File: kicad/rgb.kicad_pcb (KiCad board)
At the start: 2 copper layers, 74 x 44 mm, 33 parts, among them J1 1935776, J2 Conn_01x05, J3 Conn_01x05, J4 Conn_01x04, J5 Conn_01x02, Q1 DMG9926USD, Q2 DMG9926USD, Q3 DMG9926USD, Q4 DMG9926USD, SW1 SW_Push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

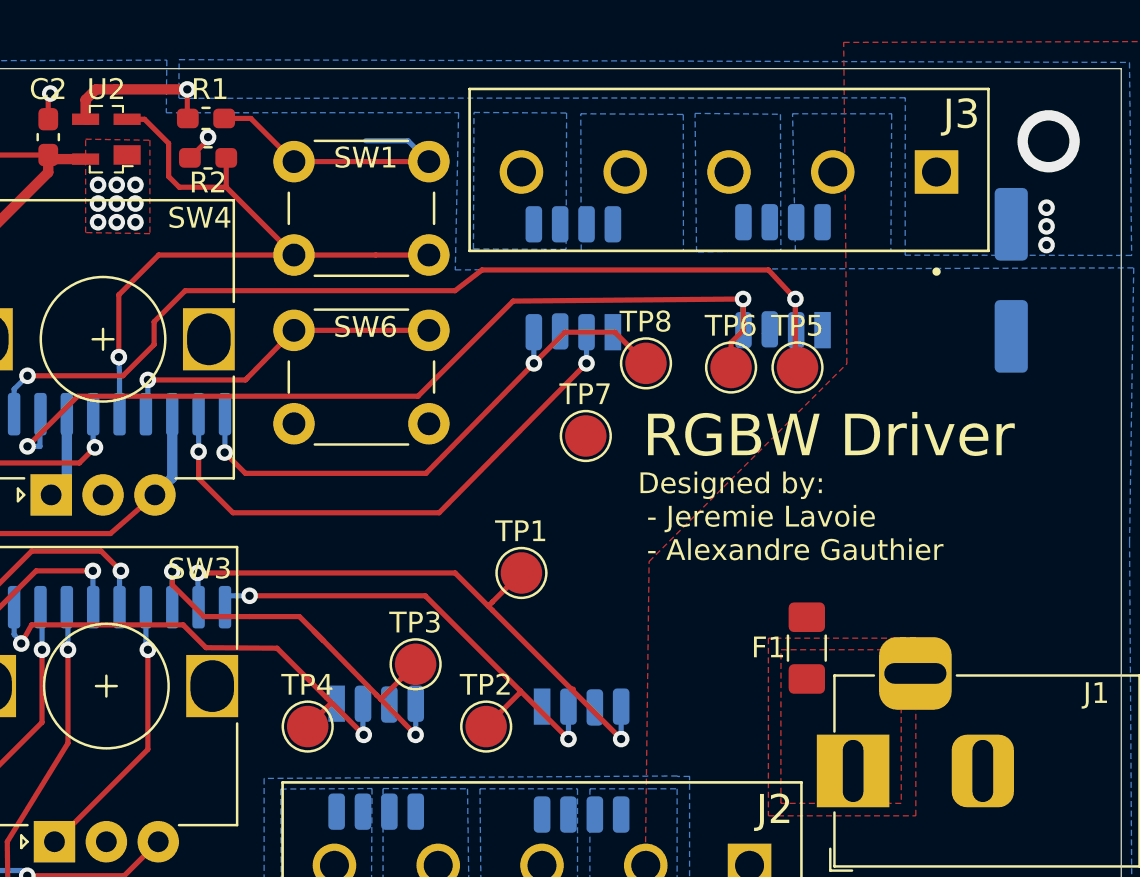
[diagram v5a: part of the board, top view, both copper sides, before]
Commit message: datasheets and model numbers
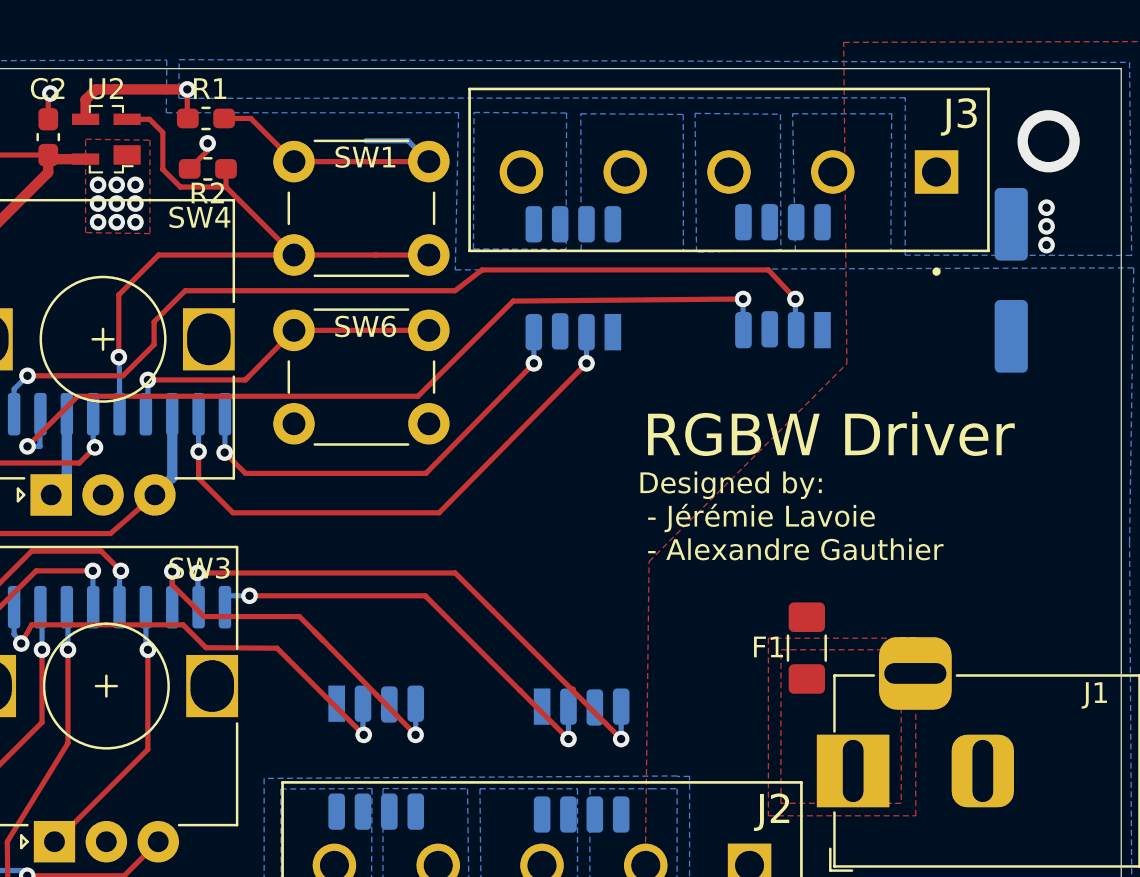
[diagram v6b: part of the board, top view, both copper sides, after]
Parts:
- removed TP1, TP2, TP3, TP4, TP5, TP6, TP7, TP8: TestPoint, TestPoint:TestPoint_Pad_D2.0mm
- SW2, SW3, SW4, SW5: value Rotary_Encoder -> PEC12R-4220F-N0024
- moved R2 0.53 mm to (152.0, 61.8)
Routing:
- net /PWM_8: track 27.5 -> 20.9 mm
- net /PWM_6: track 46.3 -> 42.0 mm
- net /PWM_5: track 47.3 -> 43.9 mm
- net /PWM_2: track 23.1 -> 20.7 mm
- net /PWM_3: track 21.8 -> 19.4 mm
- net /PWM_1: track 29.3 -> 27.0 mm
- net /PWM_4: track 24.9 -> 22.7 mm
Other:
- board text added: "Designed by: - Jérémie Lavoie - Alexandre Gauthier"
- board text removed: "Designed by: - Jeremie Lavoie - Alexandre Gauthier"

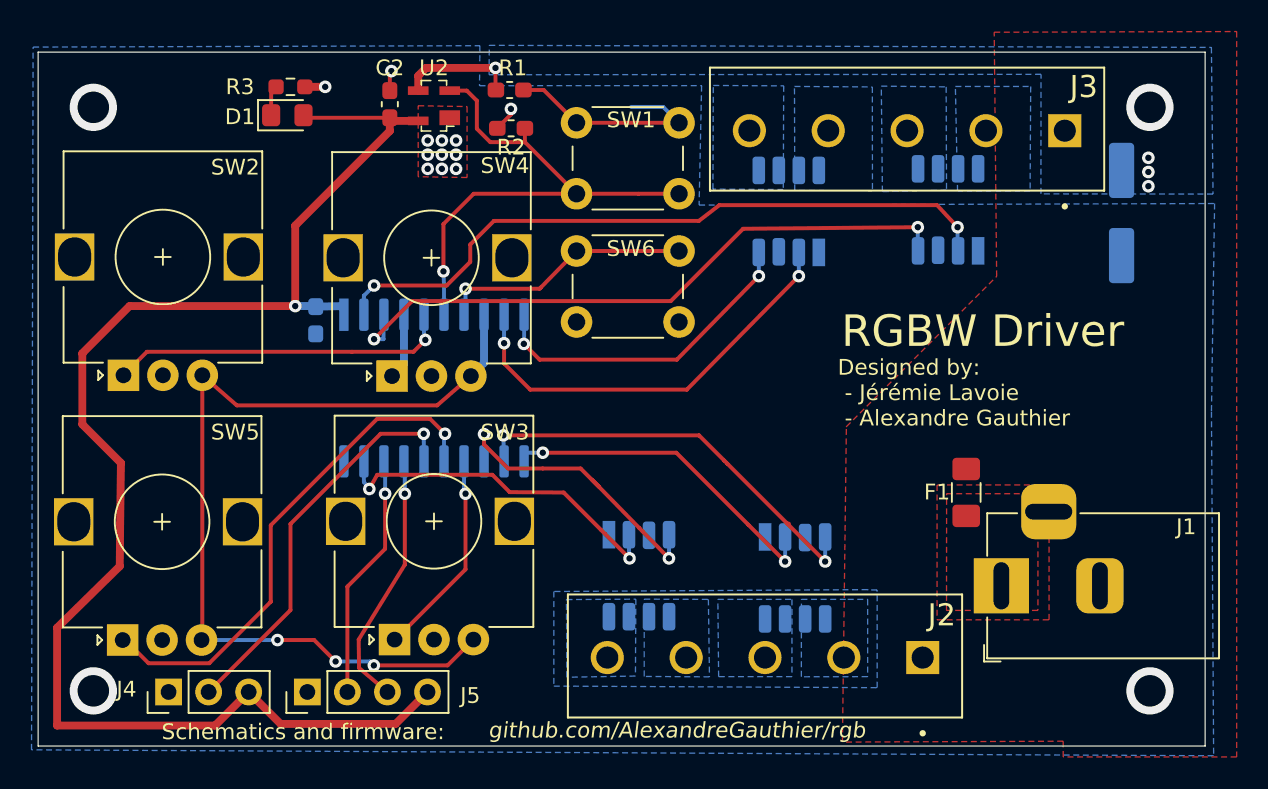
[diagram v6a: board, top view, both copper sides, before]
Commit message: changed vin connector, touchups
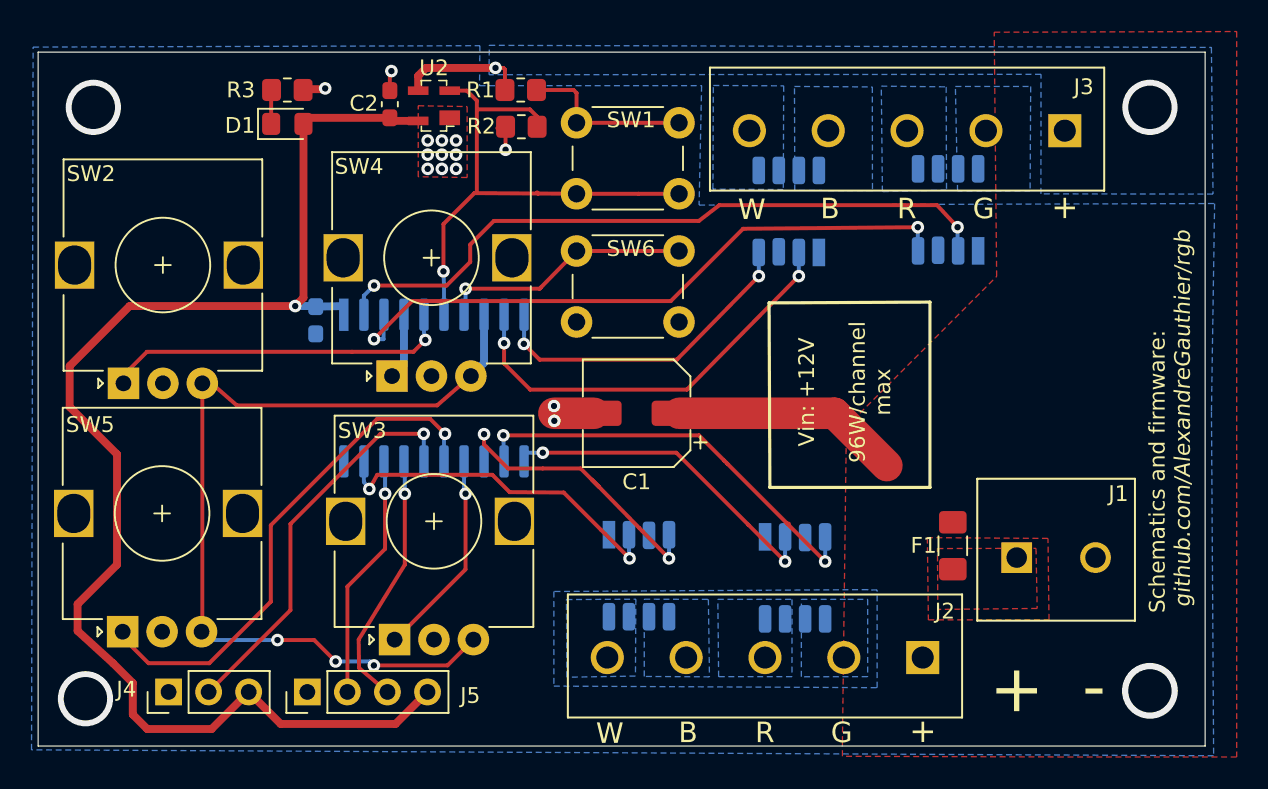
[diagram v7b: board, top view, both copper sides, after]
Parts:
- C1: moved to F.Cu
- D1: value LED -> 732-4987-2-ND
- J1: footprint rgb_footprints:barrel jack -> rgb_footprints:CUI_TB001-500-02BE
- J2, J3: value Conn_01x05 -> 102-6164-ND
- R1: value 100k -> 110k; footprint Resistor_SMD:R_0603_1608Metric_Pad1.05x0.95mm_HandSolder -> Resistor_SMD:R_0805_2012Metric_Pad1.20x1.40mm_HandSolder
- R2: footprint Resistor_SMD:R_0603_1608Metric_Pad1.05x0.95mm_HandSolder -> Resistor_SMD:R_0805_2012Metric_Pad1.20x1.40mm_HandSolder
- R3: footprint Resistor_SMD:R_0603_1608Metric_Pad0.98x0.95mm_HandSolder -> Resistor_SMD:R_0805_2012Metric_Pad1.20x1.40mm_HandSolder
- SW1, SW6: value SW_Push -> 450-1642-ND
- U2: value MIC5203 -> 576-1256-2-ND
- moved C1 33.3 mm to (159.9, 79.9), turned to 180 degrees
- moved J1 8.00 mm to (184.1, 89.0), turned to 0 degrees
- moved F1 3.49 mm to (180.0, 88.3)
- moved R1 0.70 mm to (152.6, 59.4)
- moved R2 0.66 mm to (152.6, 61.7)
- moved D1 0.55 mm to (137.8, 61.5)
- moved SW5 0.53 mm to (129.9, 85.5)
- moved SW2 0.51 mm to (129.9, 69.8)
- moved R3 0.28 mm to (137.8, 59.4)
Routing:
- net +12V: track 7.74 -> 22.8 mm, vias 4 -> 1
- net +5V: track 92.2 -> 86.3 mm
- net Net-(R1-Pad1): track 15.3 -> 12.2 mm
- net GND: track 5.06 -> 7.50 mm, vias 12 -> 14
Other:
- board text added: "+"
- board text added: "-"
- board text added: "B"
- board text added: "G"
- board text added: "R"
- board text added: "Vin: +12V 96W/channel max"
- board text added: "W"

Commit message: layout done
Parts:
- added R1: 0.005, Resistor_SMD:R_1020_2550Metric_Pad1.33x5.20mm_HandSolder, F.Cu at (192.5, 79.4)
- added R2: 10k, Resistor_SMD:R_0805_2012Metric_Pad1.20x1.40mm_HandSolder, F.Cu at (161.8, 80.2)
- added U1: ZXCT1109, Package_TO_SOT_SMD:SOT-23, F.Cu at (186.1, 79.8)
- C1: value 220 uF -> 3300 uF; footprint Capacitor_SMD:CP_Elec_6.3x7.7 -> Capacitor_THT:CP_Radial_D12.5mm_P5.00mm; moved to B.Cu
- R4: renamed from R2; value 50k -> 50 kΩ
- U2: value 576-1256-2-ND -> MIC5203-5.0
- moved C1 22.5 mm to (182.4, 80.8), turned to 90 degrees
- moved F1 13.3 mm to (192.6, 84.3)
- moved J1 2.20 mm to (183.6, 86.9)
- moved Q2 0.11 mm to (160.2, 90.2)
- moved Q1 0.11 mm to (170.1, 90.3)
- moved Q3 0.10 mm to (179.7, 67.1)
- moved Q4 0.10 mm to (169.6, 67.0)
- renumbered C2 to C3, C3 to C4, R1 to R3, R3 to R5, U1 to U3
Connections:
- F1 pad 1: +12V -> Net-(F1-Pad1)
- SW2 pad A: /SW2_A -> /SW_A1
- SW2 pad B: /SW_B -> /SW_B1
- SW3 pad A: /SW3_A -> /SW_A1
- SW3 pad B: /SW_B -> /SW_B2
- SW4 pad A: /SW4_A -> /SW_A2
- SW4 pad B: /SW_B -> /SW_B1
- SW5 pad A: /SW5_A -> /SW_A2
- SW5 pad B: /SW_B -> /SW_B2
- U3 pad 14: /SW3_A -> /SW_B1
- U3 pad 15: /SW5_A -> /SW_B2
- U3 pad 4: /SW4_A -> /SW_A1
- U3 pad 5: /SW2_A -> /SW_A2
- U3 pad 7: /SW6 -> /SENSE
- U3 pad 8: /SW_B -> /SW6
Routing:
- net /SW_A1: track 0.00 -> 60.0 mm, vias 0 -> 4
- net /SW_B: track 58.5 -> 0.00 mm, vias 3 -> 0
- net /SENSE: track 0.00 -> 42.6 mm, vias 0 -> 3
- net /SW5_A: track 32.7 -> 0.00 mm, vias 1 -> 0
- net /SW_B1: track 0.00 -> 32.4 mm, vias 0 -> 4
- net /SW_A2: track 0.00 -> 31.8 mm, vias 0 -> 1
- net /SW_B2: track 0.00 -> 31.1 mm, vias 0 -> 4
- net +12V: track 22.8 -> 52.0 mm, vias 1 -> 0
- net /SW2_A: track 22.3 -> 0.00 mm, vias 1 -> 0
- net /SW3_A: track 13.4 -> 0.00 mm, vias 1 -> 0
- net Net-(F1-Pad1): track 0.00 -> 7.21 mm
- net /SW4_A: track 4.20 -> 0.00 mm
- net +5V: track 86.3 -> 84.5 mm
- net /SW6: track 16.3 -> 14.9 mm
- net GND: track 7.50 -> 6.16 mm, vias 14 -> 13
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- added copper zone on F.Cu, net Net-(F1-Pad1)
- removed copper zone on B.Cu, net +12V
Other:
- board text added: "rev0"
- board text removed: "Schematics and firmware:"
- board text removed: "Vin: +12V 96W/channel max"
